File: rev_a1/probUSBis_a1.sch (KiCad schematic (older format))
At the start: 22 parts

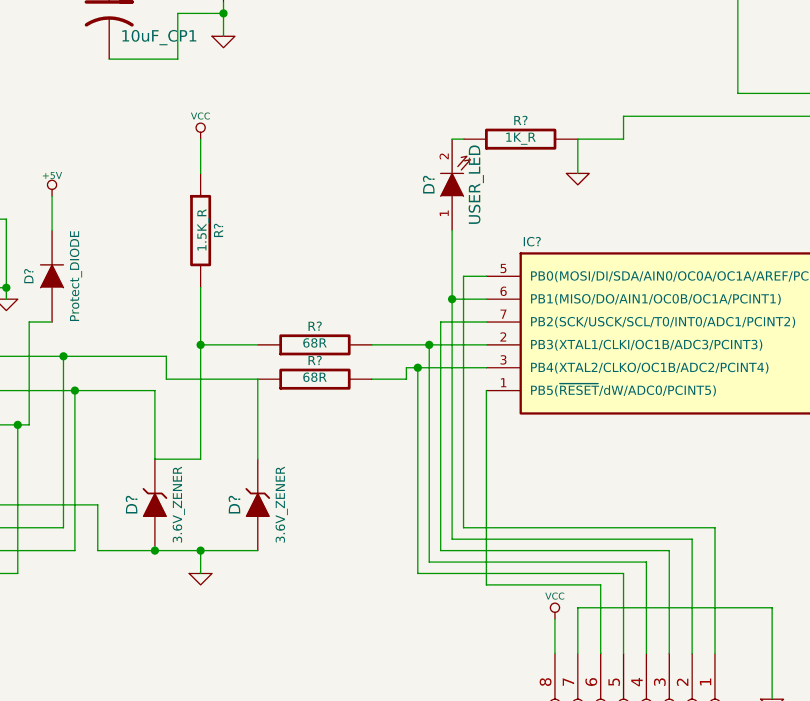
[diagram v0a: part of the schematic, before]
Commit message: added jumper for user led on PB1
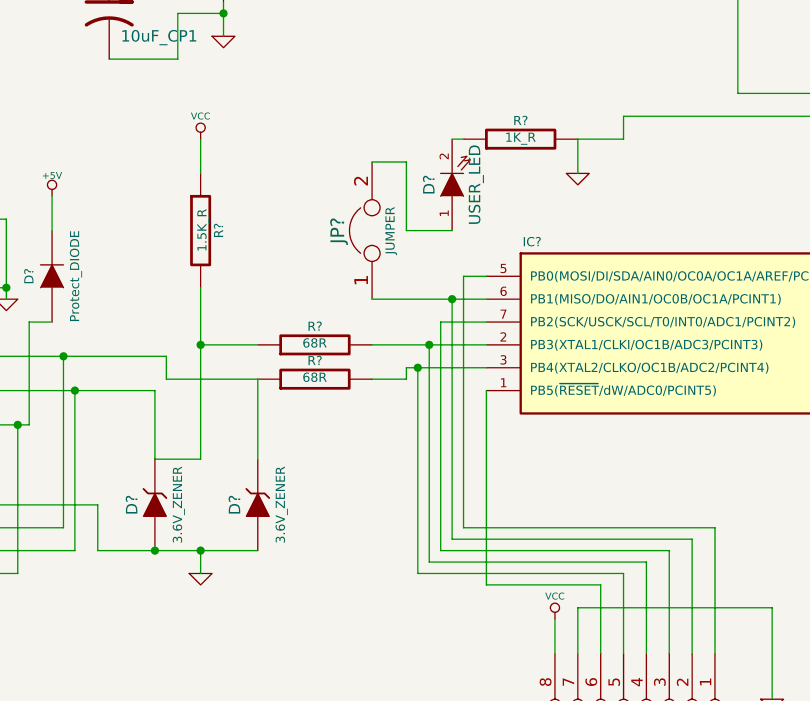
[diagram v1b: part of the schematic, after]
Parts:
- added JP?: JUMPER, symbol JUMPER
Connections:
- net at IC?.6 (PB1(MISO/DO/AIN1/OC0B/OC1A/PCINT1)), P?.2 (P2): now also JP?.1; no longer D?.1 (A)
- new net: D?.1 (A), JP?.2
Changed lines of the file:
@@
 LIBS:contrib
 LIBS:valves
+LIBS:probUSBis_a1-cache
 EELAYER 24 0
 EELAYER END
@@
 	5550 4600 5550 5150
 Wire Wire Line
-	4550 3600 4400 3600
-Wire Wire Line
-	4400 3300 4400 4650
+	4050 3600 4550 3600
 Wire Wire Line
 	4400 4650 5450 4650
@@
 	3200 2350 3400 2350
 Connection ~ 3400 2350
+$Comp
+L JUMPER JP?
+U 1 1 5406AD07
+P 4050 3300
+F 0 "JP?" H 4050 3450 60  0000 C CNN
+F 1 "JUMPER" H 4050 3220 40  0000 C CNN
+F 2 "" H 4050 3300 60  0000 C CNN
+F 3 "" H 4050 3300 60  0000 C CNN
+	1    4050 3300
+	0    -1   -1   0
+$EndComp
+Wire Wire Line
+	4400 4650 4400 3600
+Wire Wire Line
+	4050 3000 4200 3000
+Wire Wire Line
+	4200 3000 4200 3300
+Wire Wire Line
+	4200 3300 4400 3300
 $EndSCHEMATC

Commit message: made netlist
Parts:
- gave numbers to parts that had none: 23
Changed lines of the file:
@@
 $EndDescr
 $Comp
-L ATTINY85-P IC?
+L ATTINY85-P IC1
 U 1 1 5406436D
 P 5900 3750
-F 0 "IC?" H 4750 4150 40  0000 C CNN
+F 0 "IC1" H 4750 4150 40  0000 C CNN
 F 1 "ATTINY85-P" H 6900 3350 40  0000 C CNN
 F 2 "DIP8" H 6900 3750 35  0000 C CIN
@@
 $EndComp
 $Comp
-L LM78L05ACZ U?
+L LM78L05ACZ U1
 U 1 1 540646C9
 P 3400 2050
-F 0 "U?" H 3200 2250 40  0000 C CNN
+F 0 "U1" H 3200 2250 40  0000 C CNN
 F 1 "LM78L05ACZ" H 3400 2250 40  0000 L CNN
 F 2 "TO-92" H 3400 2150 30  0000 C CIN
@@
 $EndComp
 $Comp
-L GND #PWR?
+L GND #PWR15
 U 1 1 5406470F
 P 7250 4150
-F 0 "#PWR?" H 7250 4150 30  0001 C CNN
+F 0 "#PWR15" H 7250 4150 30  0001 C CNN
 F 1 "GND" H 7250 4080 30  0001 C CNN
 F 2 "" H 7250 4150 60  0000 C CNN
@@
 	7250 3950 7250 4150
 $Comp
-L GND #PWR?
+L GND #PWR5
 U 1 1 54064734
 P 3400 2450
-F 0 "#PWR?" H 3400 2450 30  0001 C CNN
+F 0 "#PWR5" H 3400 2450 30  0001 C CNN
 F 1 "GND" H 3400 2380 30  0001 C CNN
 F 2 "" H 3400 2450 60  0000 C CNN
@@
 	3400 2300 3400 2450
 $Comp
-L DIODE D?
+L DIODE D4
 U 1 1 5406479C
 P 4150 2000
-F 0 "D?" H 4150 2100 40  0000 C CNN
+F 0 "D4" H 4150 2100 40  0000 C CNN
 F 1 "DIODE" H 4150 1900 40  0000 C CNN
 F 2 "" H 4150 2000 60  0000 C CNN
@@
 	3000 2000 2800 2000
 $Comp
-L +5V #PWR?
+L +5V #PWR6
 U 1 1 54064836
 P 4550 1950
-F 0 "#PWR?" H 4550 2040 20  0001 C CNN
+F 0 "#PWR6" H 4550 2040 20  0001 C CNN
 F 1 "+5V" H 4550 2040 30  0000 C CNN
 F 2 "" H 4550 1950 60  0000 C CNN
@@
 	4550 2000 4550 1950
 $Comp
-L JUMPER3 JP?
+L JUMPER3 JP2
 U 1 1 54064EE5
 P 6100 1950
-F 0 "JP?" H 6150 1850 40  0000 L CNN
+F 0 "JP2" H 6150 1850 40  0000 L CNN
 F 1 "JUMPER3" H 6100 2050 40  0000 C CNN
 F 2 "" H 6100 1950 60  0000 C CNN
@@
 $EndComp
 $Comp
-L VCC #PWR?
+L VCC #PWR11
 U 1 1 54064F25
 P 6100 2200
-F 0 "#PWR?" H 6100 2300 30  0001 C CNN
+F 0 "#PWR11" H 6100 2300 30  0001 C CNN
 F 1 "VCC" H 6100 2300 30  0000 C CNN
 F 2 "" H 6100 2200 60  0000 C CNN
@@
 	6100 2050 6100 2200
 $Comp
-L +5V #PWR?
+L +5V #PWR9
 U 1 1 54064F6B
 P 5550 1950
-F 0 "#PWR?" H 5550 2040 20  0001 C CNN
+F 0 "#PWR9" H 5550 2040 20  0001 C CNN
 F 1 "+5V" H 5550 2040 30  0000 C CNN
 F 2 "" H 5550 1950 60  0000 C CNN
@@
 	5850 1950 5550 1950
 $Comp
-L +3.3V #PWR?
+L +3.3V #PWR12
 U 1 1 54064FE3
 P 6650 1900
-F 0 "#PWR?" H 6650 1860 30  0001 C CNN
+F 0 "#PWR12" H 6650 1860 30  0001 C CNN
 F 1 "+3.3V" H 6650 2010 30  0000 C CNN
 F 2 "" H 6650 1900 60  0000 C CNN
@@
 	6650 1950 6350 1950
 $Comp
-L ZENER D?
+L ZENER D2
 U 1 1 54065093
 P 3100 4500
-F 0 "D?" H 3100 4600 50  0000 C CNN
+F 0 "D2" H 3100 4600 50  0000 C CNN
 F 1 "3.6V_ZENER" H 3100 4400 40  0000 C CNN
 F 2 "" H 3100 4500 60  0000 C CNN
@@
 $EndComp
 $Comp
-L ZENER D?
+L ZENER D3
 U 1 1 540650A2
 P 3550 4500
-F 0 "D?" H 3550 4600 50  0000 C CNN
+F 0 "D3" H 3550 4600 50  0000 C CNN
 F 1 "3.6V_ZENER" H 3550 4400 40  0000 C CNN
 F 2 "" H 3550 4500 60  0000 C CNN
@@
 $EndComp
 $Comp
-L GND #PWR?
+L GND #PWR4
 U 1 1 540650E9
 P 3300 4800
-F 0 "#PWR?" H 3300 4800 30  0001 C CNN
+F 0 "#PWR4" H 3300 4800 30  0001 C CNN
 F 1 "GND" H 3300 4730 30  0001 C CNN
 F 2 "" H 3300 4800 60  0000 C CNN
@@
 Connection ~ 3300 4700
 $Comp
-L +3.3V #PWR?
+L +3.3V #PWR13
 U 1 1 54065119
 P 6950 1850
-F 0 "#PWR?" H 6950 1810 30  0001 C CNN
+F 0 "#PWR13" H 6950 1810 30  0001 C CNN
 F 1 "+3.3V" H 6950 1960 30  0000 C CNN
 F 2 "" H 6950 1850 60  0000 C CNN
@@
 $EndComp
 $Comp
-L DIODE D?
+L DIODE D6
 U 1 1 54065142
 P 7250 1850
-F 0 "D?" H 7250 1950 40  0000 C CNN
+F 0 "D6" H 7250 1950 40  0000 C CNN
 F 1 "Si_DIODE" H 7250 1750 40  0000 C CNN
 F 2 "" H 7250 1850 60  0000 C CNN
@@
 $EndComp
 $Comp
-L DIODE D?
+L DIODE D7
 U 1 1 54065151
 P 7750 1850
-F 0 "D?" H 7750 1950 40  0000 C CNN
+F 0 "D7" H 7750 1950 40  0000 C CNN
 F 1 "Si_DIODE" H 7750 1750 40  0000 C CNN
 F 2 "" H 7750 1850 60  0000 C CNN
@@
 $EndComp
 $Comp
-L +5V #PWR?
+L +5V #PWR16
 U 1 1 5406516A
 P 8100 1800
-F 0 "#PWR?" H 8100 1890 20  0001 C CNN
+F 0 "#PWR16" H 8100 1890 20  0001 C CNN
 F 1 "+5V" H 8100 1890 30  0000 C CNN
 F 2 "" H 8100 1800 60  0000 C CNN
@@
 	7550 1850 7450 1850
 $Comp
-L USB-MINI-B CON?
+L USB-MINI-B CON1
 U 1 1 540652B1
 P 1800 3850
-F 0 "CON?" H 1550 4300 60  0000 C CNN
+F 0 "CON1" H 1550 4300 60  0000 C CNN
 F 1 "USB-MINI-B" H 1750 3350 60  0000 C CNN
 F 2 "" H 1800 3850 60  0000 C CNN
@@
 $EndComp
 $Comp
-L R R?
+L R R3
 U 1 1 540652C5
 P 3800 3950
-F 0 "R?" V 3880 3950 40  0000 C CNN
+F 0 "R3" V 3880 3950 40  0000 C CNN
 F 1 "68R" V 3807 3951 40  0000 C CNN
 F 2 "" V 3730 3950 30  0000 C CNN
@@
 $EndComp
 $Comp
-L R R?
+L R R2
 U 1 1 540652D7
 P 3800 3800
-F 0 "R?" V 3880 3800 40  0000 C CNN
+F 0 "R2" V 3880 3800 40  0000 C CNN
 F 1 "68R" V 3807 3801 40  0000 C CNN
 F 2 "" V 3730 3800 30  0000 C CNN
@@
 	3100 4000 3100 4300
 $Comp
-L GND #PWR?
+L GND #PWR1
 U 1 1 540653CF
 P 2450 3600
-F 0 "#PWR?" H 2450 3600 30  0001 C CNN
+F 0 "#PWR1" H 2450 3600 30  0001 C CNN
 F 1 "GND" H 2450 3530 30  0001 C CNN
 F 2 "" H 2450 3600 60  0000 C CNN
@@
 	2350 4150 2550 4150
 $Comp
-L R R?
+L R R1
 U 1 1 540654DB
 P 3300 3300
-F 0 "R?" V 3380 3300 40  0000 C CNN
+F 0 "R1" V 3380 3300 40  0000 C CNN
 F 1 "1.5K_R" V 3307 3301 40  0000 C CNN
 F 2 "" V 3230 3300 30  0000 C CNN
@@
 Connection ~ 3300 3800
 $Comp
-L VCC #PWR?
+L VCC #PWR3
 U 1 1 5406551F
 P 3300 2900
-F 0 "#PWR?" H 3300 3000 30  0001 C CNN
+F 0 "#PWR3" H 3300 3000 30  0001 C CNN
 F 1 "VCC" H 3300 3000 30  0000 C CNN
 F 2 "" H 3300 2900 60  0000 C CNN
@@
 	3300 3050 3300 2900
 $Comp
-L VCC #PWR?
+L VCC #PWR14
 U 1 1 54065550
 P 7250 3350
-F 0 "#PWR?" H 7250 3450 30  0001 C CNN
+F 0 "#PWR14" H 7250 3450 30  0001 C CNN
 F 1 "VCC" H 7250 3450 30  0000 C CNN
 F 2 "" H 7250 3350 60  0000 C CNN
@@
 	7250 3350 7250 3550
 $Comp
-L C C?
+L C C2
 U 1 1 54065627
 P 7250 3750
-F 0 "C?" H 7250 3850 40  0000 L CNN
+F 0 "C2" H 7250 3850 40  0000 L CNN
 F 1 "100nF_C" H 7256 3665 40  0000 L CNN
 F 2 "" H 7288 3600 30  0000 C CNN
@@
 Connection ~ 7250 3500
 $Comp
-L CONN_4 P?
+L CONN_4 P1
 U 1 1 5406575D
 P 1950 4650
-F 0 "P?" V 1900 4650 50  0000 C CNN
+F 0 "P1" V 1900 4650 50  0000 C CNN
 F 1 "USB_A_MALE" V 2000 4650 50  0000 C CNN
 F 2 "" H 1950 4650 60  0000 C CNN
@@
 Connection ~ 2500 4150
 $Comp
-L +5V #PWR?
+L +5V #PWR2
 U 1 1 54066922
 P 2650 3150
-F 0 "#PWR?" H 2650 3240 20  0001 C CNN
+F 0 "#PWR2" H 2650 3240 20  0001 C CNN
 F 1 "+5V" H 2650 3240 30  0000 C CNN
 F 2 "" H 2650 3150 60  0000 C CNN
@@
 	2650 3150 2650 3300
 $Comp
-L DIODE D?
+L DIODE D1
 U 1 1 54066975
 P 2650 3500
-F 0 "D?" H 2650 3600 40  0000 C CNN
+F 0 "D1" H 2650 3600 40  0000 C CNN
 F 1 "Protect_DIODE" H 2650 3400 40  0000 C CNN
 F 2 "" H 2650 3500 60  0000 C CNN
@@
 	5800 4950 5800 5350
 $Comp
-L GND #PWR?
+L GND #PWR10
 U 1 1 54067278
 P 5800 5350
-F 0 "#PWR?" H 5800 5350 30  0001 C CNN
+F 0 "#PWR10" H 5800 5350 30  0001 C CNN
 F 1 "GND" H 5800 5280 30  0001 C CNN
 F 2 "" H 5800 5350 60  0000 C CNN
@@
 $EndComp
 $Comp
-L VCC #PWR?
+L VCC #PWR7
 U 1 1 54067326
 P 4850 5000
-F 0 "#PWR?" H 4850 5100 30  0001 C CNN
+F 0 "#PWR7" H 4850 5100 30  0001 C CNN
 F 1 "VCC" H 4850 5100 30  0000 C CNN
 F 2 "" H 4850 5000 60  0000 C CNN
@@
 	4850 5000 4850 5150
 $Comp
-L CONN_8 P?
+L CONN_8 P2
 U 1 1 54067469
 P 5200 5500
-F 0 "P?" V 5150 5500 60  0000 C CNN
+F 0 "P2" V 5150 5500 60  0000 C CNN
 F 1 "CONN_8" V 5250 5500 60  0000 C CNN
 F 2 "" H 5200 5500 60  0000 C CNN
@@
 $EndComp
 $Comp
-L LED D?
+L LED D5
 U 1 1 54067702
 P 4400 3100
-F 0 "D?" H 4400 3200 50  0000 C CNN
+F 0 "D5" H 4400 3200 50  0000 C CNN
 F 1 "USER_LED" H 4400 3000 50  0000 C CNN
 F 2 "" H 4400 3100 60  0000 C CNN
@@
 $EndComp
 $Comp
-L R R?
+L R R4
 U 1 1 54067711
 P 4700 2900
-F 0 "R?" V 4780 2900 40  0000 C CNN
+F 0 "R4" V 4780 2900 40  0000 C CNN
 F 1 "1K_R" V 4707 2901 40  0000 C CNN
 F 2 "" V 4630 2900 30  0000 C CNN
@@
 $EndComp
 $Comp
-L GND #PWR?
+L GND #PWR8
 U 1 1 54067720
 P 4950 3050
-F 0 "#PWR?" H 4950 3050 30  0001 C CNN
+F 0 "#PWR8" H 4950 3050 30  0001 C CNN
 F 1 "GND" H 4950 2980 30  0001 C CNN
 F 2 "" H 4950 3050 60  0000 C CNN
@@
 Connection ~ 1250 3550
 $Comp
-L CONN_4 P?
+L CONN_4 P3
 U 1 1 54067AAD
 P 6850 2750
-F 0 "P?" V 6800 2750 50  0000 C CNN
+F 0 "P3" V 6800 2750 50  0000 C CNN
 F 1 "CONN_4" V 6900 2750 50  0000 C CNN
 F 2 "" H 6850 2750 60  0000 C CNN
@@
 	5150 2900 4950 2900
 $Comp
-L LED D?
+L LED D8
 U 1 1 54067C92
 P 7850 3600
-F 0 "D?" H 7850 3700 50  0000 C CNN
+F 0 "D8" H 7850 3700 50  0000 C CNN
 F 1 "ON_LED" H 7850 3500 50  0000 C CNN
 F 2 "" H 7850 3600 60  0000 C CNN
@@
 $EndComp
 $Comp
-L R R?
+L R R5
 U 1 1 54067CB0
 P 7600 3950
-F 0 "R?" V 7680 3950 40  0000 C CNN
+F 0 "R5" V 7680 3950 40  0000 C CNN
 F 1 "1K_R" V 7607 3951 40  0000 C CNN
 F 2 "" V 7530 3950 30  0000 C CNN
@@
 Connection ~ 7250 3400
 $Comp
-L CP1 C?
+L CP1 C1
 U 1 1 54067E1E
 P 2900 2350
-F 0 "C?" H 2950 2450 50  0000 L CNN
+F 0 "C1" H 2950 2450 50  0000 L CNN
 F 1 "10uF_CP1" H 2950 2250 50  0000 L CNN
 F 2 "" H 2900 2350 60  0000 C CNN
@@
 Connection ~ 3400 2350
 $Comp
-L JUMPER JP?
+L JUMPER JP1
 U 1 1 5406AD07
 P 4050 3300
-F 0 "JP?" H 4050 3450 60  0000 C CNN
+F 0 "JP1" H 4050 3450 60  0000 C CNN
 F 1 "JUMPER" H 4050 3220 40  0000 C CNN
 F 2 "" H 4050 3300 60  0000 C CNN
